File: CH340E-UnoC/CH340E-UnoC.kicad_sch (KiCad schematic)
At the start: 45 parts, among them IC1 NCP1117ST50T3G/1.0A, IC2 AP7366-33W5-7/600mA, J1 Power, J2 Digital/PWM, J3 Analog, J4 Digital/PWM, J5 USB_C-31-M-12_USB2.0, Q1 FDN340P, SW1 TS42, U1 LMV358IDGKR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

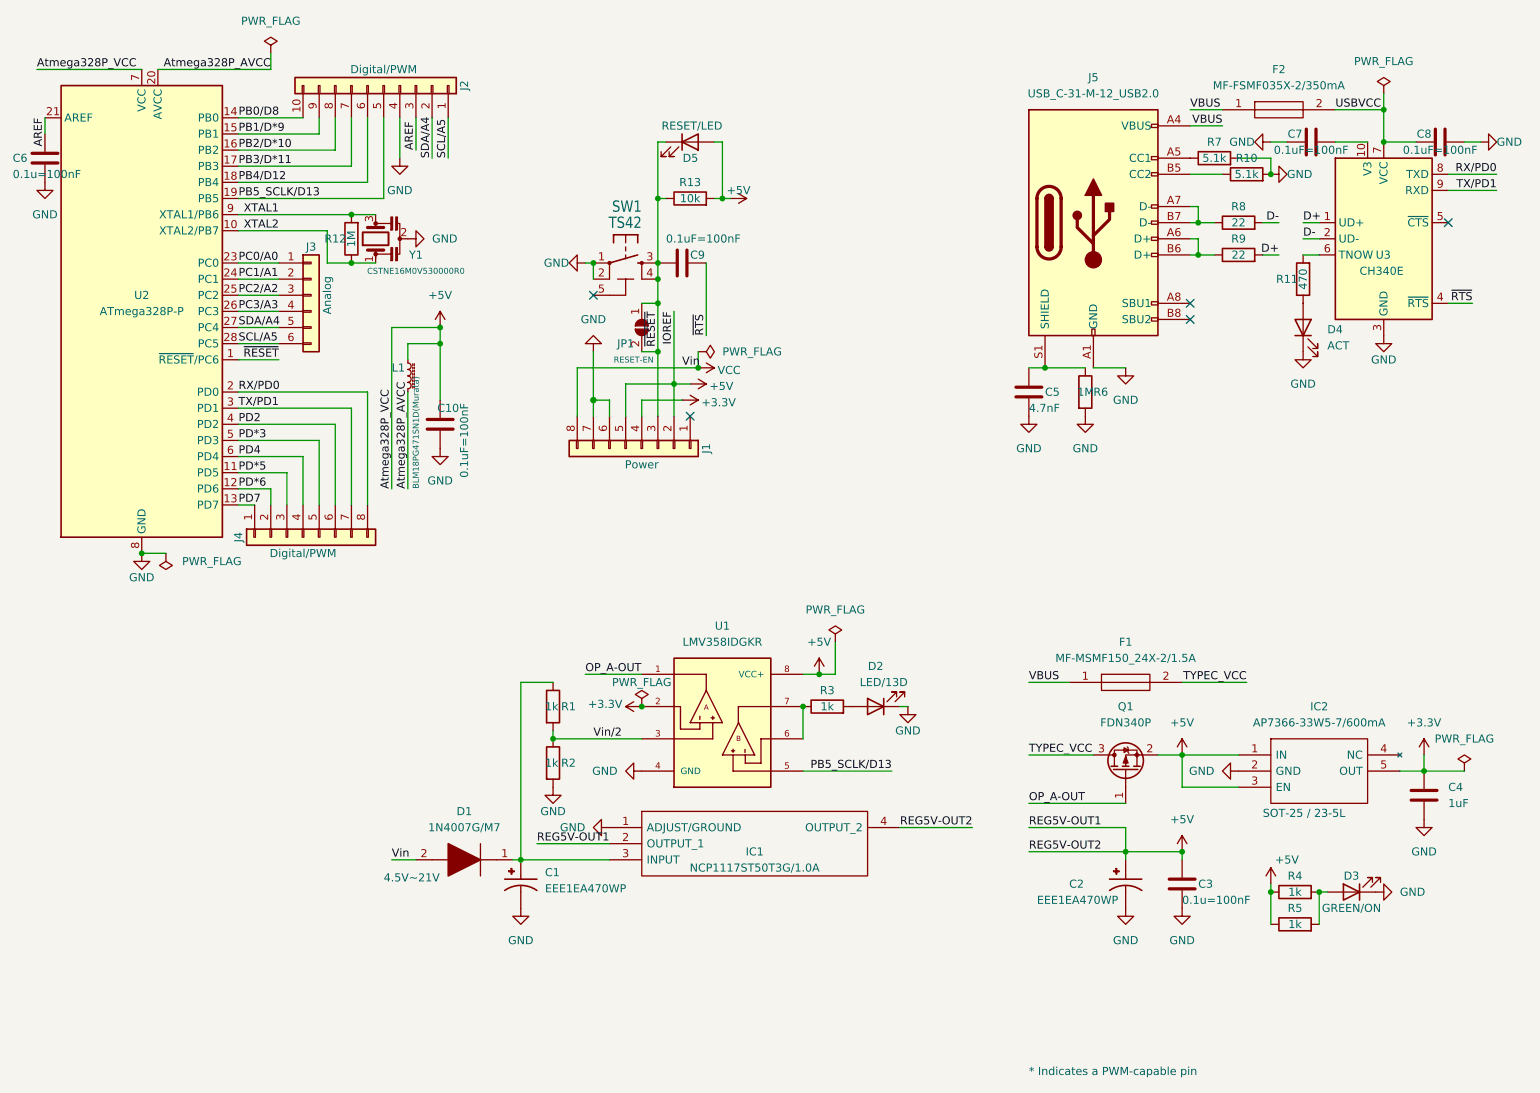
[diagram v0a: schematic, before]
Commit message: feat: Add part symbols.
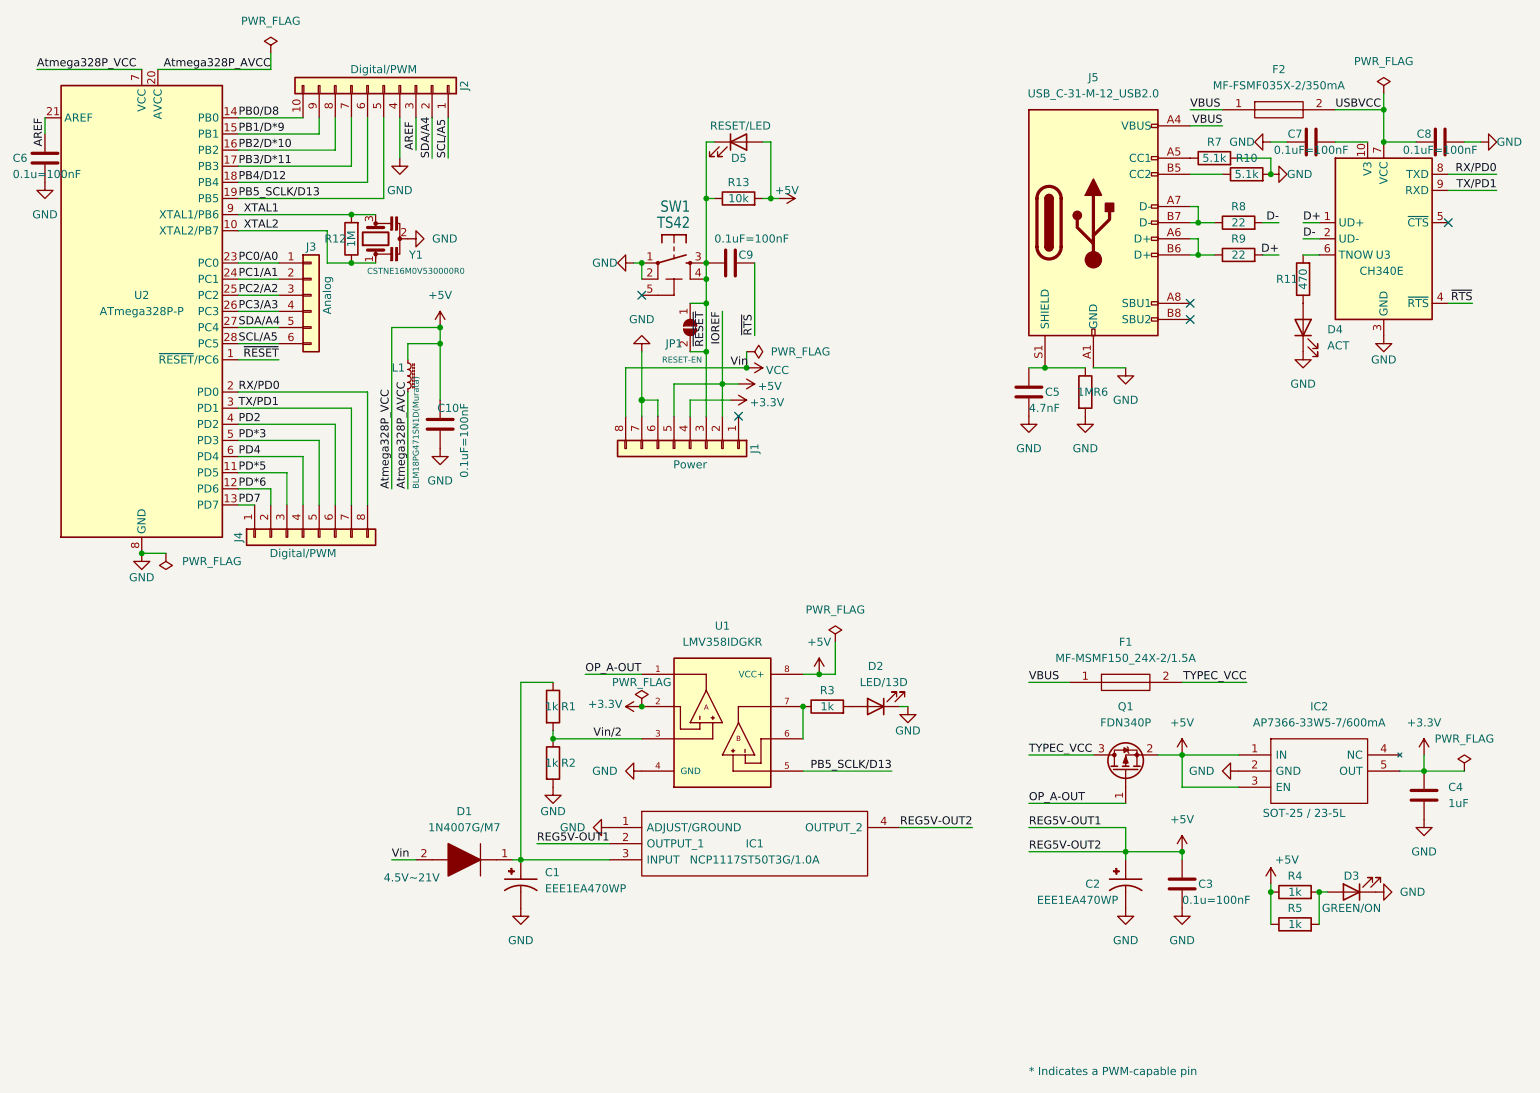
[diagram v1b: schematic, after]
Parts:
- removed C1, C2: EEE1EA470WP, CAP_EEE1EA470WP, symbol Capacitors-EEE1EA470WP_SnapEDA:EEE1EA470WP
- removed D1: 1N4007G/M7, DIOM5025X220N, symbol Diode-1N4007G_SamacSys:1N4007G
- removed F1: MF-MSMF150_24X-2/1.5A, FUSC4632X160N, symbol Fuse_MF-MSMF150_24X-2_1812 (4532 Metric)_SamacSys:MF-MSMF150_24X-2
- removed F2: MF-FSMF035X-2/350mA, FUSC1608X65N, symbol Fuse_MF-FSMF035X-2_SamacSys:MF-FSMF035X-2
- removed IC1: NCP1117ST50T3G/1.0A, SOT230P700X180-4N, symbol IC-Reg_NCP1117ST50T3G_SamacSys:NCP1117ST50T3G
- removed IC2: AP7366-33W5-7/600mA, SOT95P285X130-5N, symbol IC-Reg_AP7366-33W5-7_SamacSys:AP7366-33W5-7
- removed U1: LMV358IDGKR, SOP65P490X110-8N, symbol OPAmpDual_LMV358IDGKR_SnapEDA:LMV358IDGKR
- added C1, C2: EEE1EA470WP, CAP_EEE1EA470WP, symbol EEE1EA470WP:EEE1EA470WP
- added D1: 1N4007G/M7, DIOM5025X220N, symbol 1N4007G:1N4007G
- added F1: MF-MSMF150_24X-2/1.5A, FUSC4632X160N, symbol MF-MSMF150_24X-2:MF-MSMF150_24X-2
- added F2: MF-FSMF035X-2/350mA, FUSC1608X65N, symbol MF-FSMF035X-2:MF-FSMF035X-2
- added IC1: NCP1117ST50T3G/1.0A, SOT230P700X180-4N, symbol NCP1117ST50T3G:NCP1117ST50T3G
- added IC2: AP7366-33W5-7/600mA, SOT95P285X130-5N, symbol AP7366-33W5-7:AP7366-33W5-7
- added U1: LMV358IDGKR, SOP65P490X110-8N, symbol LMV358IDGKR:LMV358IDGKR
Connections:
- net +3.3V: now also IC2.5 (OUT)
- net +3V3: now also U1.2
- net +5V: now also C2.1, IC1.2 (OUTPUT_1), IC1.4 (OUTPUT_2), IC2.1 (IN), IC2.3 (EN), U1.8 (VCC+)
- net GND: now also C1.2, C2.2, IC1.1 (ADJUST/GROUND), IC2.2 (GND), U1.4 (GND)
- net OP_A-OUT: now also U1.1
- net PB5_SCLK/D13: now also U1.5
- net TYPEC_VCC: now also F1.2
- net USBVCC: now also F2.2
- net VBUS: now also F1.1, F2.1
- net VCC: now also D1.2
- net Vin/2: now also U1.3
- net at R3.1: now also U1.6, U1.7
- net at R1.1: now also C1.1, D1.1, IC1.3 (INPUT)
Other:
- moved on the sheet: C9, D5, J1, JP1, R13, SW1
